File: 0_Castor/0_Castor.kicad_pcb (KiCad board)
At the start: 2 copper layers, 135.3 x 172.8 mm, 179 parts, among them J1 Conn_01x02, SW1 Battery Switch, SW2 LED Switch, SW3 Reset Switch, U1 Nice_Nano_V2

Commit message: feat: convert 3.3V from nice!nano to 5V to LEDs
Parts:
- removed SW3: Reset Switch, Button_Switch_SMD:Panasonic_EVQPUL_EVQPUC
- added C45: 100µF, Capacitor_SMD:C_0603_1608Metric, F.Cu at (244.8, 131.0)
- added C46: 100µF, Capacitor_SMD:C_0603_1608Metric, F.Cu at (244.8, 133.5)
- added C47: 1nF, Capacitor_SMD:C_0603_1608Metric, F.Cu at (244.8, 136.0)
- added C48: 100nF, Capacitor_SMD:C_0603_1608Metric, F.Cu at (244.8, 138.5)
- added C49: 100nF, Capacitor_SMD:C_0603_1608Metric, F.Cu at (244.8, 141.0)
- added L1: 2.2µH, Inductor_SMD:L_1210_3225Metric, F.Cu at (254.8, 129.0)
- added R3: 180kΩ, Resistor_SMD:R_0603_1608Metric, F.Cu at (258.5, 148.5)
- added R4: 20kΩ, Resistor_SMD:R_0603_1608Metric, F.Cu at (258.5, 151.0)
- added U2: TLV61070ADBV, Package_TO_SOT_SMD:SOT-23-6, F.Cu at (255.5, 137.5)
- added U3: TXU0101DBVR, Package_TO_SOT_SMD:SOT-23-6, F.Cu at (266.6, 139.8)
- C1: footprint Capacitor_SMD:C_0402_1005Metric -> Capacitor_SMD:C_0603_1608Metric
- C10, C11, C12, C13, C14, C15, C16, C17, C18, C19, C2, C20, C21, C22, C23, C24, C25, C26, C27, C28, C29, C3, C30, C31, C32, C33, C34, C35, C36, C37, C38, C39, C4, C40, C41, C42, C43, C44, C5, C6, C7, C8, C9: footprint Capacitor_SMD:C_0402_1005Metric -> Capacitor_SMD:C_0603_1608Metric; moved to F.Cu
- R1, R2: footprint Resistor_SMD:R_0402_1005Metric -> Resistor_SMD:R_0603_1608Metric
- SW2: value LED Switch -> Reset Switch; footprint davidphilipbarr:SPDT_C128955 -> Button_Switch_SMD:Panasonic_EVQPUL_EVQPUC
- moved C20 36.2 mm to (229.5, 129.2), turned to 0 degrees
- moved C29 34.0 mm to (233.5, 129.2), turned to 0 degrees
- moved C30 33.2 mm to (233.5, 131.8), turned to 0 degrees
- moved C38 33.0 mm to (237.5, 129.2), turned to 0 degrees
- moved C39 32.3 mm to (237.5, 131.8), turned to 0 degrees
- moved C40 31.5 mm to (237.5, 134.3), turned to 0 degrees
- moved C2 27.1 mm to (221.5, 129.2), turned to 0 degrees
- moved C3 26.5 mm to (221.5, 131.8), turned to 0 degrees
- moved C4 25.9 mm to (221.5, 134.3), turned to 0 degrees
- moved C5 25.3 mm to (221.5, 136.8), turned to 0 degrees
- moved C6 24.7 mm to (221.5, 139.3), turned to 0 degrees
- moved C7 24.1 mm to (221.5, 141.8), turned to 0 degrees
- moved C8 23.6 mm to (221.5, 144.3), turned to 0 degrees
- moved C9 23.0 mm to (221.5, 146.8), turned to 0 degrees
- moved C10 22.5 mm to (221.5, 149.3), turned to 0 degrees
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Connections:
- C1 pad 1: VDD -> +5V_{LED}
- C10 pad 1: VDD -> +5V_{LED}
- C11 pad 1: VDD -> +5V_{LED}
- C12 pad 1: VDD -> +5V_{LED}
- C13 pad 1: VDD -> +5V_{LED}
- C14 pad 1: VDD -> +5V_{LED}
- C15 pad 1: VDD -> +5V_{LED}
- C16 pad 1: VDD -> +5V_{LED}
- C17 pad 1: VDD -> +5V_{LED}
- C18 pad 1: VDD -> +5V_{LED}
- C19 pad 1: VDD -> +5V_{LED}
- C2 pad 1: VDD -> +5V_{LED}
- C20 pad 1: VDD -> +5V_{LED}
- C21 pad 1: VDD -> +5V_{LED}
- C22 pad 1: VDD -> +5V_{LED}
- C23 pad 1: VDD -> +5V_{LED}
- C24 pad 1: VDD -> +5V_{LED}
- C25 pad 1: VDD -> +5V_{LED}
- C26 pad 1: VDD -> +5V_{LED}
- C27 pad 1: VDD -> +5V_{LED}
- C28 pad 1: VDD -> +5V_{LED}
- C29 pad 1: VDD -> +5V_{LED}
- C3 pad 1: VDD -> +5V_{LED}
- C30 pad 1: VDD -> +5V_{LED}
- C31 pad 1: VDD -> +5V_{LED}
- C32 pad 1: VDD -> +5V_{LED}
- C33 pad 1: VDD -> +5V_{LED}
- C34 pad 1: VDD -> +5V_{LED}
- C35 pad 1: VDD -> +5V_{LED}
- C36 pad 1: VDD -> +5V_{LED}
- C37 pad 1: VDD -> +5V_{LED}
- C38 pad 1: VDD -> +5V_{LED}
- C39 pad 1: VDD -> +5V_{LED}
- C4 pad 1: VDD -> +5V_{LED}
- C40 pad 1: VDD -> +5V_{LED}
- C41 pad 1: VDD -> +5V_{LED}
- C42 pad 1: VDD -> +5V_{LED}
- C43 pad 1: VDD -> +5V_{LED}
- C44 pad 1: VDD -> +5V_{LED}
- C5 pad 1: VDD -> +5V_{LED}
- C6 pad 1: VDD -> +5V_{LED}
- C7 pad 1: VDD -> +5V_{LED}
- C8 pad 1: VDD -> +5V_{LED}
- C9 pad 1: VDD -> +5V_{LED}
- LED1 pad 3: VDD -> +5V_{LED}
- LED10 pad 3: VDD -> +5V_{LED}
- LED11 pad 3: VDD -> +5V_{LED}
- LED12 pad 3: VDD -> +5V_{LED}
- LED13 pad 3: VDD -> +5V_{LED}
- LED14 pad 3: VDD -> +5V_{LED}
- LED15 pad 3: VDD -> +5V_{LED}
- LED16 pad 3: VDD -> +5V_{LED}
- LED17 pad 3: VDD -> +5V_{LED}
- LED18 pad 3: VDD -> +5V_{LED}
- LED19 pad 3: VDD -> +5V_{LED}
- LED2 pad 3: VDD -> +5V_{LED}
- LED20 pad 3: VDD -> +5V_{LED}
- LED21 pad 3: VDD -> +5V_{LED}
- LED22 pad 3: VDD -> +5V_{LED}
- LED23 pad 3: VDD -> +5V_{LED}
- LED24 pad 3: VDD -> +5V_{LED}
- LED25 pad 3: VDD -> +5V_{LED}
- LED26 pad 3: VDD -> +5V_{LED}
- LED27 pad 3: VDD -> +5V_{LED}
- LED28 pad 3: VDD -> +5V_{LED}
- LED29 pad 3: VDD -> +5V_{LED}
- LED3 pad 3: VDD -> +5V_{LED}
- LED30 pad 3: VDD -> +5V_{LED}
- LED31 pad 3: VDD -> +5V_{LED}
- LED32 pad 3: VDD -> +5V_{LED}
- LED33 pad 3: VDD -> +5V_{LED}
- LED34 pad 3: VDD -> +5V_{LED}
- LED35 pad 3: VDD -> +5V_{LED}
- LED36 pad 3: VDD -> +5V_{LED}
- LED37 pad 3: VDD -> +5V_{LED}
- LED38 pad 3: VDD -> +5V_{LED}
- LED39 pad 3: VDD -> +5V_{LED}
- LED4 pad 3: VDD -> +5V_{LED}
- LED40 pad 3: VDD -> +5V_{LED}
- LED41 pad 3: VDD -> +5V_{LED}
- LED42 pad 3: VDD -> +5V_{LED}
- LED43 pad 3: VDD -> +5V_{LED}
- LED44 pad 3: VDD -> +5V_{LED}
- LED5 pad 3: VDD -> +5V_{LED}
- LED6 pad 3: VDD -> +5V_{LED}
- LED7 pad 3: VDD -> +5V_{LED}
- LED8 pad 3: VDD -> +5V_{LED}
- LED9 pad 3: VDD -> +5V_{LED}
- R1 pad 2: /LED IN -> /LEDs/Voltage booster/D_{5V}
- SW1 pad 2: /RAW -> +3.7V
- SW2 pad 1: /RAW -> GND
- SW2 pad 2: VDD -> /RST
- U1 pad 1: /LED IN -> /LED_{IN}
- U1 pad 21: unconnected-(U1-3.3v-Pad21) -> +3.3V_{Nano}
- U1 pad 24: /RAW -> +3.7V

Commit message: feat: add voltage booster for LEDs power supply
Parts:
- added R5: 1kΩ, Resistor_SMD:R_0603_1608Metric, F.Cu at (246.0, 157.0)
- added R6: 5Ω, Resistor_SMD:R_0603_1608Metric, F.Cu at (246.0, 150.0)
- added R7: 5MΩ, Resistor_SMD:R_0603_1608Metric, F.Cu at (246.0, 152.5)
- C46: value 100µF -> 1µF
- R3: value 180kΩ -> 184kΩ
- U3: value TXU0101DBVR -> TXU0101DBV
- moved U3 11.5 mm to (255.6, 143.3)
- moved U2 0.46 mm to (255.6, 137.1)
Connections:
- C45 pad 1: +3.3V_{Nano} -> +3.7_{Battery}
- C46 pad 1: +5V_{LED} -> Net-(U2-V_{OUT})
- C47 pad 1: +5V_{LED} -> Net-(U2-V_{OUT})
- C49 pad 2: +5V_{LED} -> +5V
- L1 pad 1: +3.3V_{Nano} -> Net-(U2-EN)
- R1 pad 2: /LEDs/Voltage booster/D_{5V} -> /LEDs/Voltage booster/5V_{INPUT}
- R3 pad 1: +5V_{LED} -> Net-(U2-V_{OUT})
- SW1 pad 2: +3.7V -> +3.7_{Battery}
- U1 pad 24: +3.7V -> +3.7_{Battery}
- U2 pad 3: +3.3V_{Nano} -> Net-(U2-EN)
- U2 pad 5: +5V_{LED} -> Net-(U2-V_{OUT})
- U2 pad 6: +3.3V_{Nano} -> Net-(U2-EN)
- U3 pad 4: /LEDs/Voltage booster/D_{5V} -> /LEDs/Voltage booster/5V_{INPUT}
- U3 pad 5: /LEDs/Voltage booster/D_{5V} -> +3.3V_{Nano}
- U3 pad 6: +5V_{LED} -> +5V

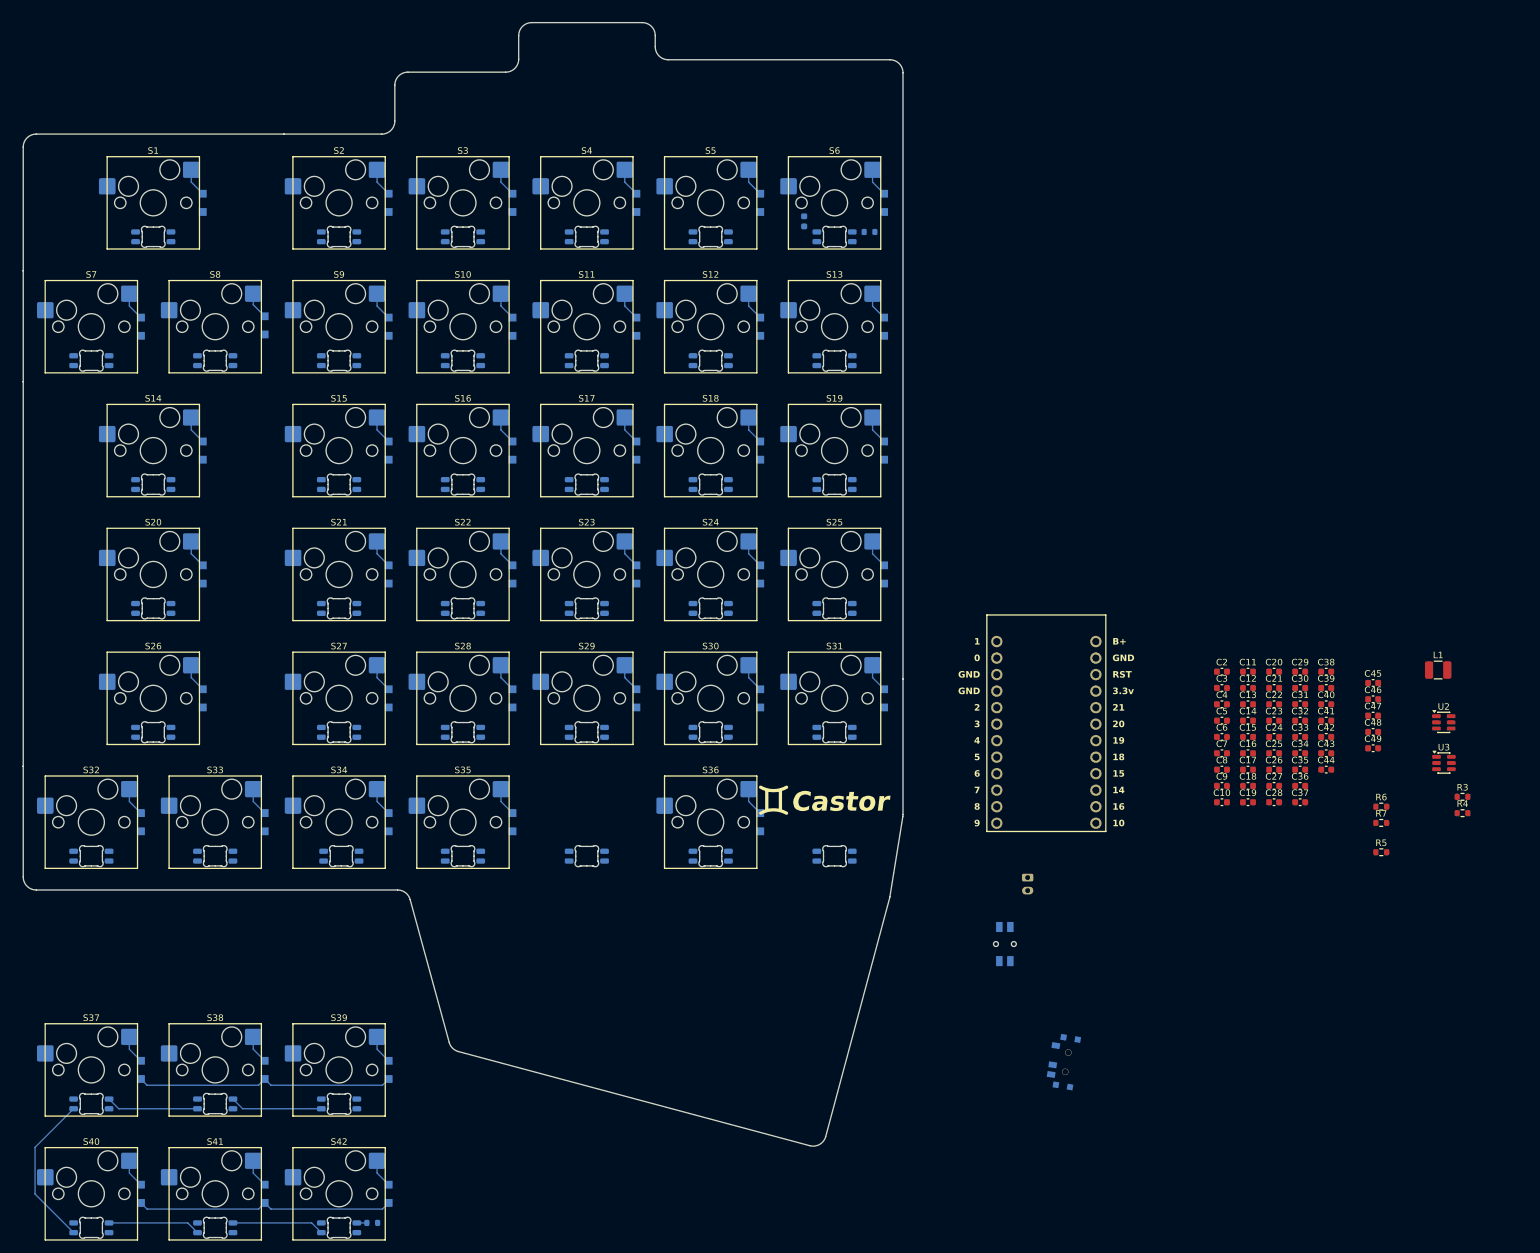
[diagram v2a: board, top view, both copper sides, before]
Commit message: feat: remove LED's and place components in PCB
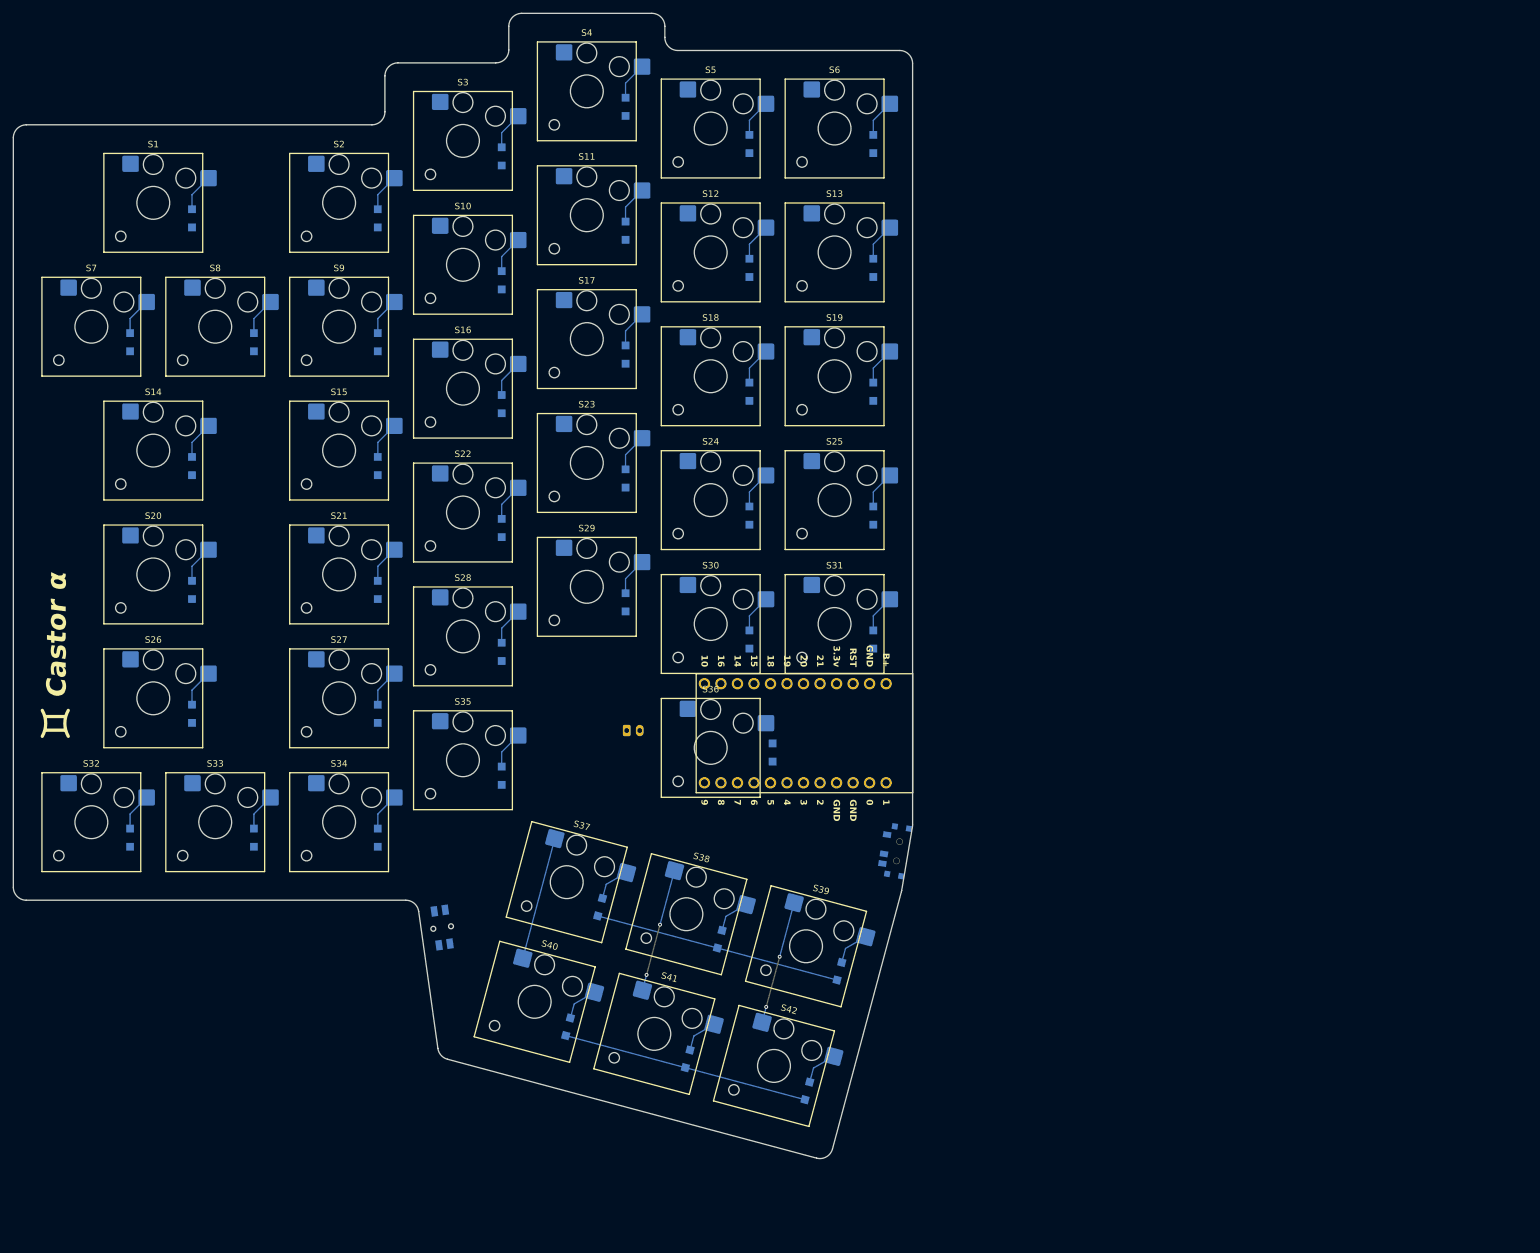
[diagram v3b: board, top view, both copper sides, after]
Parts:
- removed C1, C10, C11, C12, C13, C14, C15, C16, C17, C18, C19, C2, C20, C21, C22, C23, C24, C25, C26, C27, C28, C29, C3, C30, C31, C32, C33, C34, C35, C36, C37, C38, C39, C4, C40, C41, C42, C43, C44, C48, C49, C5, C6, C7, C8, C9: 100nF, Capacitor_SMD:C_0603_1608Metric
- removed C45: 100µF, Capacitor_SMD:C_0603_1608Metric
- removed C46: 1µF, Capacitor_SMD:C_0603_1608Metric
- removed C47: 1nF, Capacitor_SMD:C_0603_1608Metric
- removed L1: 2.2µH, Inductor_SMD:L_1210_3225Metric
- removed LED1, LED10, LED11, LED12, LED13, LED14, LED15, LED16, LED17, LED18, LED19, LED2, LED20, LED21, LED22, LED23, LED24, LED25, LED26, LED27, LED28, LED29, LED3, LED30, LED31, LED32, LED33, LED34, LED35, LED36, LED37, LED38, LED39, LED4, LED40, LED41, LED42, LED43, LED44, LED5, LED6, LED7, LED8, LED9: SK6812MINI-E, LED_SMD:LED_SK6812MINI-E_3.2x2.8mm_P1.5mm_ReverseMount
- removed R1, R2: 500Ω, Resistor_SMD:R_0603_1608Metric
- removed R3: 184kΩ, Resistor_SMD:R_0603_1608Metric
- removed R4: 20kΩ, Resistor_SMD:R_0603_1608Metric
- removed R5: 1kΩ, Resistor_SMD:R_0603_1608Metric
- removed R6: 5Ω, Resistor_SMD:R_0603_1608Metric
- removed R7: 5MΩ, Resistor_SMD:R_0603_1608Metric
- removed U2: TLV61070ADBV, Package_TO_SOT_SMD:SOT-23-6
- removed U3: TXU0101DBV, Package_TO_SOT_SMD:SOT-23-6
- S1, S14, S20, S26: footprint ScottoKeebs_Hotswap:Hotswap_MX_2.00u -> ScottoKeebs_Hotswap:Hotswap_Choc_V2_2.00u
- S10, S11, S12, S13, S15, S16, S17, S18, S19, S2, S21, S22, S23, S24, S25, S27, S28, S29, S3, S30, S31, S32, S33, S34, S35, S37, S38, S39, S4, S40, S41, S42, S5, S6, S7, S8, S9: footprint ScottoKeebs_Hotswap:Hotswap_MX_1.00u -> ScottoKeebs_Hotswap:Hotswap_Choc_V2_1.00u
- S36: footprint ScottoKeebs_Hotswap:Hotswap_MX_3.00u -> ScottoKeebs_Hotswap:Hotswap_Choc_V2_3.00u
- U1: moved to B.Cu
- moved SW2 86.6 mm to (101.6, 168.6), turned to -82.02 degrees
- moved S37 78.6 mm to (120.7, 161.6), turned to -15 degrees
- moved S38 76.3 mm to (139.1, 166.6), turned to -15 degrees
- moved D37 74.9 mm to (125.9, 165.5), turned to 75 degrees
- moved S40 74.3 mm to (115.8, 180.0), turned to -15 degrees
- moved S39 74.3 mm to (157.5, 171.5), turned to -15 degrees
- moved D38 72.8 mm to (144.3, 170.4), turned to 75 degrees
- moved S41 71.9 mm to (134.2, 185.0), turned to -15 degrees
- moved D39 71.0 mm to (162.7, 175.3), turned to 75 degrees
- moved D40 70.5 mm to (120.9, 183.9), turned to 75 degrees
- moved S42 69.7 mm to (152.6, 189.9), turned to -15 degrees
- moved D41 68.3 mm to (139.3, 188.8), turned to 75 degrees
- moved D42 66.3 mm to (157.7, 193.7), turned to 75 degrees
- moved J1 65.7 mm to (130.0, 138.3), turned to 0 degrees
- moved SW1 41.5 mm to (171.7, 156.9)
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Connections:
- U1 pad 1: /LED_{IN} -> unconnected-(U1-Pad1)
- U1 pad 21: +3.3V_{Nano} -> unconnected-(U1-3.3v-Pad21)
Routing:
- net Net-(LED41-DOUT): track 24.0 -> 0.00 mm
- net /Column 5: track 0.00 -> 19.1 mm, vias 0 -> 2
- net /Column 6: track 0.00 -> 19.1 mm, vias 0 -> 2
- net /Column 4: track 0.00 -> 19.0 mm
- net Net-(LED42-DOUT): track 14.2 -> 0.00 mm
- net Net-(LED40-DOUT): track 14.2 -> 0.00 mm
- net Net-(LED43-DOUT): track 14.2 -> 0.00 mm
- net Net-(LED39-DOUT): track 14.2 -> 0.00 mm
- net Net-(D36-A): track 4.42 -> 0.00 mm
- net Net-(LED44-DOUT): track 1.86 -> 0.00 mm
- net Net-(D8-A): track 4.21 -> 5.84 mm
- net /Row 7: track 39.7 -> 38.1 mm
- net /Row 6: track 39.7 -> 38.1 mm
- net Net-(D41-A): track 4.42 -> 5.84 mm
- net Net-(D40-A): track 4.42 -> 5.84 mm
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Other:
- board size 135.3 x 172.8 mm -> 138.3 x 176.1 mm
- board text added: "Castor α"
- board text removed: "Castor"

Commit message: feat: route left side PCB
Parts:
- moved U1 0.81 mm to (156.2, 137.9)
- moved SW1 0.71 mm to (171.0, 156.8), turned to 80.4 degrees
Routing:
- net /Column 2: track 0.00 -> 299.3 mm, vias 0 -> 6
- net /Column 4: track 19.0 -> 293.0 mm, vias 0 -> 6
- net /Column 3: track 0.00 -> 273.9 mm, vias 0 -> 6
- net /Column 0: track 0.00 -> 237.1 mm
- net /Row 0: track 0.00 -> 209.2 mm
- net /Row 1: track 0.00 -> 199.3 mm
- net /Column 1: track 0.00 -> 194.6 mm
- net /Column 6: track 19.1 -> 207.8 mm, vias 2 -> 7
- net /Row 2: track 0.00 -> 172.6 mm
- net /Row 3: track 0.00 -> 155.5 mm
- net /Column 5: track 19.1 -> 172.3 mm, vias 2 -> 8
- net /Row 5: track 0.00 -> 119.4 mm, vias 0 -> 1
- net /Row 4: track 0.00 -> 119.1 mm
- net GND: track 0.00 -> 100.6 mm, vias 0 -> 4
- net /RST: track 0.00 -> 94.8 mm, vias 0 -> 3
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
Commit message: feat: add mounting holes to left side
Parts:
- added REF**: Mounting Hole, AstralExtensions:Mounting Hole, F.Cu at (152.4, 55.2)
- added REF**: Mounting Hole, AstralExtensions:Mounting Hole, F.Cu at (113.8, 95.2)
- added REF**: Mounting Hole, AstralExtensions:Mounting Hole, F.Cu at (158.4, 156.0)
- added REF**: Mounting Hole, AstralExtensions:Mounting Hole, F.Cu at (57.1, 67.1)
- added REF**: Mounting Hole, AstralExtensions:Mounting Hole, F.Cu at (103.6, 158.4)
- added REF**: Mounting Hole, AstralExtensions:Mounting Hole, F.Cu at (57.1, 143.2)
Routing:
- net /RST: track 94.8 -> 101.9 mm
- net GND: track 100.6 -> 106.1 mm, vias 4 -> 2
